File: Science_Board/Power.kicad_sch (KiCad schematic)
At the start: 57 parts, among them IC1 TCKE603RA, IC2 TCKE603RA, IC3 TCKE603RM, J21 Molex_Megafit_02, J22 Molex_Megafit_02, J3 Molex_Megafit_02, J4 Molex_Megafit_02, Q1 BS250, Q2 NMOS, Q3 NMOS, Q4 NMOS, U1 AP63205WU

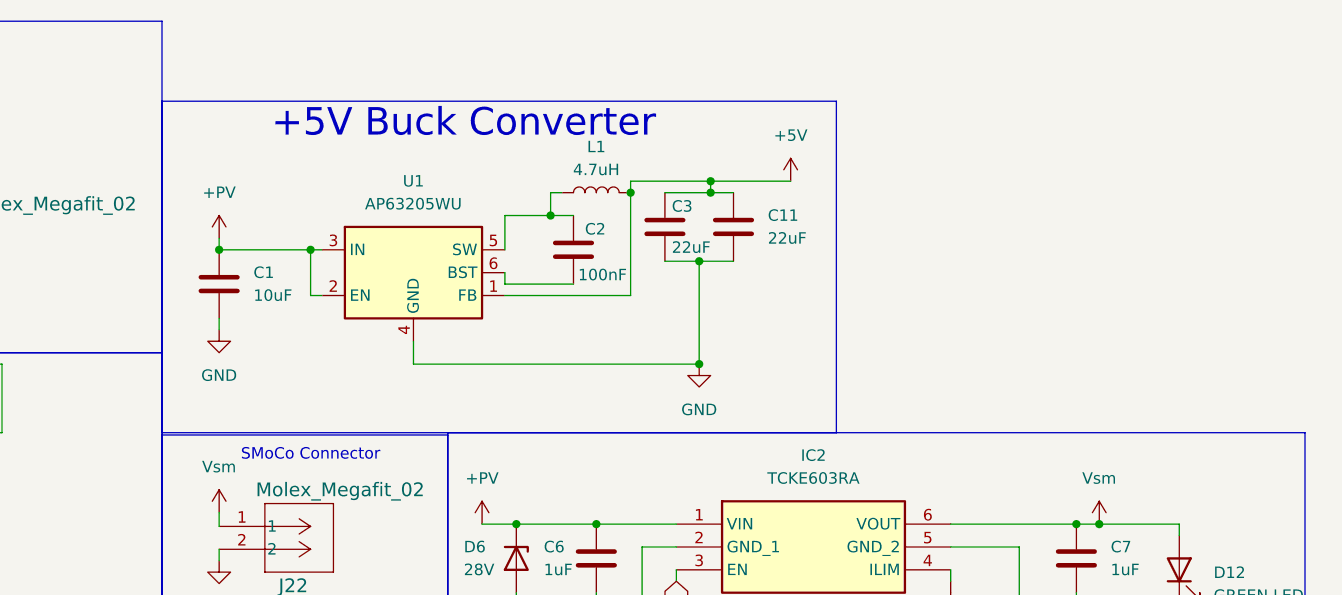
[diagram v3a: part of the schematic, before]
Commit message: changed the buck to the correct footprint
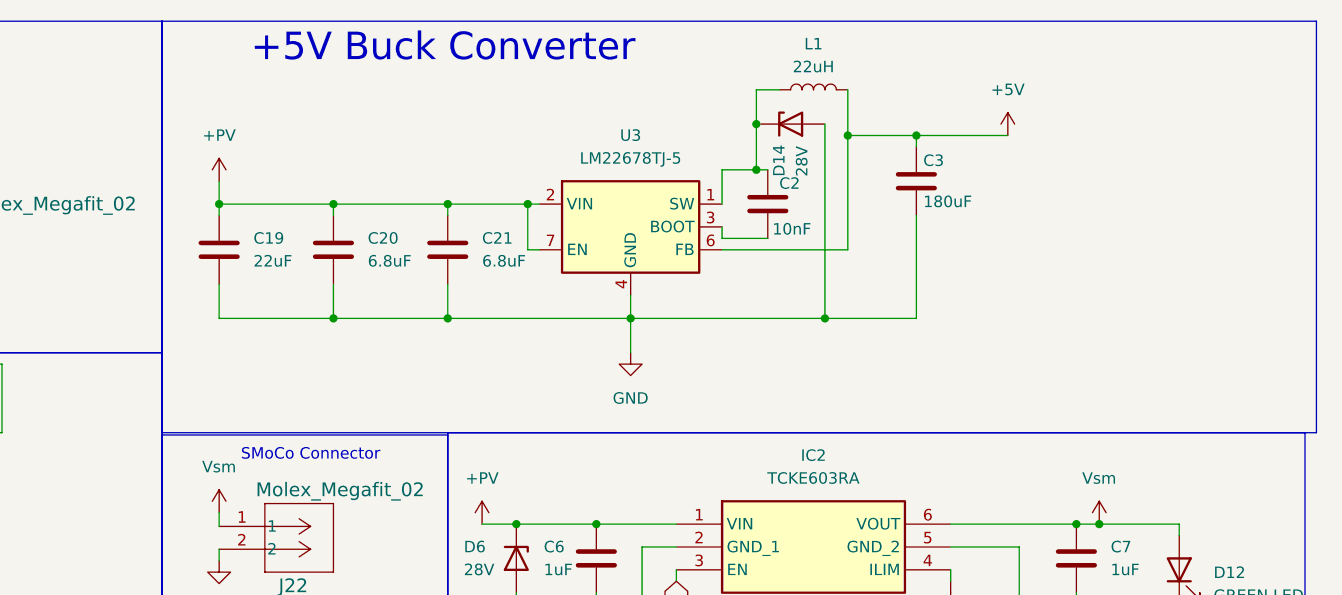
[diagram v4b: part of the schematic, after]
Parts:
- removed C1: 10uF, Capacitor_SMD:C_0603_1608Metric_Pad1.08x0.95mm_HandSolder, symbol Device:C
- removed C11: 22uF, Capacitor_SMD:C_0603_1608Metric_Pad1.08x0.95mm_HandSolder, symbol Device:C
- removed U1: AP63205WU, Package_TO_SOT_SMD:TSOT-23-6, symbol Regulator_Switching:AP63205WU
- added C19: 22uF, Capacitor_SMD:C_0603_1608Metric_Pad1.08x0.95mm_HandSolder, symbol Device:C
- added C20, C21: 6.8uF, Capacitor_SMD:C_0603_1608Metric_Pad1.08x0.95mm_HandSolder, symbol Device:C
- added D14: 28V, Diode_SMD:D_SOD-123, symbol Device:D_Zener
- added U3: LM22678TJ-5, Package_TO_SOT_SMD:TO-263-7_TabPin8, symbol Regulator_Switching:LM22678TJ-5
- C2: value 100nF -> 10nF
- C3: value 22uF -> 180uF
- L1: value 4.7uH -> 22uH
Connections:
- net +5V: now also U3.6 (FB)
- net +PV: now also C19.1, C20.1, C21.1, U3.2 (VIN), U3.7 (EN)
- net GND: now also C19.2, C20.2, C21.2, D14.2 (A), U3.4 (GND), U3.8 (GND)
- net at C2.1, L1.1: now also D14.1 (K), U3.1 (SW)
- net at C2.2: now also U3.3 (BOOT)
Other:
- moved on the sheet: C2, C3, L1

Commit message: real inductor
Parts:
- L1: value 22uH -> 6.8uH; footprint Inductor_SMD:L_0603_1608Metric_Pad1.05x0.95mm_HandSolder -> Inductor_SMD:L_Bourns_SRN8040TA
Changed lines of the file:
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@@
 			)
 		)
-		(property "Value" "22uH"
+		(property "Value" "6.8uH"
 			(at 228.6 17.78 90)
 			(show_name no)
@@
 			)
 		)
-		(property "Footprint" "Inductor_SMD:L_0603_1608Metric_Pad1.05x0.95mm_HandSolder"
+		(property "Footprint" "Inductor_SMD:L_Bourns_SRN8040TA"
 			(at 228.6 20.32 0)
 			(hide yes)
@@
 			)
 		)
-		(property "Datasheet" ""
+		(property "Datasheet" "https://www.digikey.com/en/products/detail/bourns-inc/SRN8040TA-6R8M/6155128?s=N4IgjCBcoEwAwA4DsVQGMoDMCGAbAzgKYA0IA9lANogCsAdAGwAEArQBIin0ysdd0BmXp1qCALMP4T2I%2BjUmikC%2BgmV0AnAuYzSDOmC10eOkHqEm90vqbryLjQ0vur7mk044BdUgAcALlAgAKoAdgCWfgDymACyhNj4AK4AToQgAL6k8AgIqCAYkDgEJORUogYAgrKCTFXeIP6BoRHRcQkpaZkgALQQ0PlYeESkFJDUYGC5nuldNHk%2BUGC%2BC5AwNDNAA"
 			(at 228.6 20.32 0)
 			(hide yes)

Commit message: fix mosfet
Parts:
- Q1: footprint Package_TO_SOT_THT:TO-92_Inline -> Package_TO_SOT_SMD:SOT-223
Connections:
- net at D1.2 (A), R1.2: now also Q1.1 (G); no longer Q1.2 (G)
- net at J21.1: now also Q1.2 (D), Q1.4 (D); no longer Q1.1 (D)
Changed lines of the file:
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@@
 	)
 	(junction
+		(at 132.08 58.42)
+		(diameter 0)
+		(color 0 0 0 0)
+	)
+	(junction
 		(at 111.76 64.77)
 		(diameter 0)
@@
 	(wire
 		(pts
+			(xy 132.08 55.88) (xy 132.08 58.42)
+		)
+		(stroke
+			(width 0)
+			(type default)
+		)
+	)
+	(wire
+		(pts
 			(xy 191.77 68.58) (xy 195.58 68.58)
 		)
@@
 			)
 		)
-		(property "Footprint" "Package_TO_SOT_THT:TO-92_Inline"
+		(property "Footprint" "Package_TO_SOT_SMD:SOT-223"
 			(at 125.095 55.88 0)
 			(hide yes)
@@
 			)
 		)
-		(property "Datasheet" "http://www.vishay.com/docs/70209/70209.pdf"
+		(property "Datasheet" "https://www.digikey.com/en/products/detail/onsemi/NDT452AP/458901"
 			(at 123.19 55.88 0)
 			(hide yes)
@@
 		(pin "1"
 		)
+		(pin "2"
+		)
+		(pin "4"
+		)
 		(instances

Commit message: added temp connector =
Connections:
- net +PV: no longer J3.1, J4.1
- net +Vpre: now reaches J21.1, Q1.2 (D), Q1.4 (D)
- net +Vpre: now also J3.1, J4.1
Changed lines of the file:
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@@
 	)
 	(junction
+		(at 106.68 30.48)
+		(diameter 0)
+		(color 0 0 0 0)
+	)
+	(junction
 		(at 140.97 149.86)
 		(diameter 0)
@@
 	(wire
 		(pts
+			(xy 106.68 26.67) (xy 106.68 30.48)
+		)
+		(stroke
+			(width 0)
+			(type default)
+		)
+	)
+	(wire
+		(pts
 			(xy 16.51 114.3) (xy 16.51 118.11)
 		)
@@
 	)
 	(symbol
+		(lib_id "power:VCC")
+		(at 83.82 115.57 0)
+		(unit 1)
+		(body_style 1)
+		(exclude_from_sim no)
+		(in_bom yes)
+		(on_board yes)
+		(in_pos_files yes)
+		(dnp no)
+		(property "Reference" "#PWR0124"
+			(at 83.82 119.38 0)
+			(hide yes)
+			(show_name no)
+			(do_not_autoplace no)
+			(effects
+				(font
+					(size 1.27 1.27)
+				)
+			)
+		)
+		(property "Value" "+Vpre"
+			(at 80.518 111.76 0)
+			(show_name no)
+			(do_not_autoplace no)
+			(effects
+				(font
+					(size 1.27 1.27)
+				)
+				(justify left)
+			)
+		)
+		(property "Footprint" "MRDT_Connectors:MOLEX_MegaFit_02_Horizontal"
+			(at 83.82 115.57 0)
+			(hide yes)
+			(show_name no)
+			(do_not_autoplace no)
+			(effects
+				(font
+					(size 1.27 1.27)
+				)
+			)
+		)
+		(property "Datasheet" ""
+			(at 83.82 115.57 0)
+			(hide yes)
+			(show_name no)
+			(do_not_autoplace no)
+			(effects
+				(font
+					(size 1.27 1.27)
+				)
+			)
+		)
+		(property "Description" "Power symbol creates a global label with name \"VCC\""
+			(at 83.82 115.57 0)
+			(hide yes)
+			(show_name no)
+			(do_not_autoplace no)
+			(effects
+				(font
+					(size 1.27 1.27)
+				)
+			)
+		)
+		(pin "1"
+		)
+		(instances
+			(project "Science_Board"
+				(path "/4f5c5f7f-4385-4de2-96ca-2ae741ebf691/6219bf49-5574-4710-86f4-9f93da84ad76"
+					(reference "#PWR0124")
+					(unit 1)
+				)
+			)
+		)
+	)
+	(symbol
 		(lib_id "Device:R_US")
 		(at 38.1 45.72 0)
@@
 	)
 	(symbol
-		(lib_id "power:VCC")
-		(at 83.82 115.57 0)
+		(lib_id "Simulation_SPICE:NMOS")
+		(at 35.56 77.47 0)
 		(unit 1)
 		(body_style 1)
@@
 		(dnp no)
 		(fields_autoplaced yes)
-		(property "Reference" "#PWR046"
-			(at 83.82 119.38 0)
-			(hide yes)
+		(property "Reference" "Q4"
+			(at 41.91 76.1999 0)
 			(show_name no)
 			(do_not_autoplace no)
@@
 					(size 1.27 1.27)
 				)
+				(justify left)
 			)
 		)
-		(property "Value" "+PV"
-			(at 83.82 110.49 0)
+		(property "Value" "NMOS"
+			(at 41.91 78.7399 0)
 			(show_name no)
 			(do_not_autoplace no)
@@
 					(size 1.27 1.27)
 				)
+				(justify left)
 			)
 		)
-		(property "Footprint" "MRDT_Connectors:MOLEX_MegaFit_02_Horizontal"
-			(at 83.82 115.57 0)
+		(property "Footprint" "Package_TO_SOT_SMD:SOT-23-3"
+			(at 40.64 74.93 0)
 			(hide yes)
 			(show_name no)
@@
 			)
 		)
-		(property "Datasheet" ""
-			(at 83.82 115.57 0)
+		(property "Datasheet" "https://ngspice.sourceforge.io/docs/ngspice-html-manual/manual.xhtml#cha_MOSFETs"
+			(at 35.56 90.17 0)
 			(hide yes)
 			(show_name no)
@@
 			)
 		)
-		(property "Description" "Power symbol creates a global label with name \"VCC\""
-			(at 83.82 115.57 0)
+		(property "Description" "N-MOSFET transistor, drain/source/gate"
+			(at 35.56 77.47 0)
 			(hide yes)
 			(show_name no)
@@
 			)
 		)
-		(pin "1"
-		)
-		(instances
-			(project "Science_Board"
-				(path "/4f5c5f7f-4385-4de2-96ca-2ae741ebf691/6219bf49-5574-4710-86f4-9f93da84ad76"
-					(reference "#PWR046")
-					(unit 1)
-				)
-			)
-		)
-	)
-	(symbol
-		(lib_id "Simulation_SPICE:NMOS")
-		(at 35.56 77.47 0)
-		(unit 1)
-		(body_style 1)
-		(exclude_from_sim no)
-		(in_bom yes)
-		(on_board yes)
-		(in_pos_files yes)
-		(dnp no)
-		(fields_autoplaced yes)
-		(property "Reference" "Q4"
-			(at 41.91 76.1999 0)
+		(property "Sim.Device" "NMOS"
+			(at 35.56 94.615 0)
+			(hide yes)
 			(show_name no)
 			(do_not_autoplace no)
@@
 					(size 1.27 1.27)
 				)
-				(justify left)
 			)
 		)
-		(property "Value" "NMOS"
-			(at 41.91 78.7399 0)
+		(property "Sim.Type" "VDMOS"
+			(at 35.56 96.52 0)
+			(hide yes)
 			(show_name no)
 			(do_not_autoplace no)
@@
 					(size 1.27 1.27)
 				)
-				(justify left)
 			)
 		)
-		(property "Footprint" "Package_TO_SOT_SMD:SOT-23-3"
-			(at 40.64 74.93 0)
+		(property "Sim.Pins" "1=D 2=G 3=S"
+			(at 35.56 92.71 0)
 			(hide yes)
 			(show_name no)
@@
 			)
 		)
-		(property "Datasheet" "https://ngspice.sourceforge.io/docs/ngspice-html-manual/manual.xhtml#cha_MOSFETs"
-			(at 35.56 90.17 0)
+		(pin "1"
+		)
+		(pin "3"
+		)
+		(pin "2"
+		)
+		(instances
+			(project "Science_Board"
+				(path "/4f5c5f7f-4385-4de2-96ca-2ae741ebf691/6219bf49-5574-4710-86f4-9f93da84ad76"
+					(reference "Q4")
+					(unit 1)
+				)
+			)
+		)
+	)
+	(symbol
+		(lib_id "power:VCC")
+		(at 38.1 71.12 0)
+		(unit 1)
+		(body_style 1)
+		(exclude_from_sim no)
+		(in_bom yes)
+		(on_board yes)
+		(in_pos_files yes)
+		(dnp no)
+		(fields_autoplaced yes)
+		(property "Reference" "#PWR091"
+			(at 38.1 74.93 0)
 			(hide yes)
 			(show_name no)
@@
 			)
 		)
-		(property "Description" "N-MOSFET transistor, drain/source/gate"
-			(at 35.56 77.47 0)
-			(hide yes)
+		(property "Value" "+3V3"
+			(at 38.1 66.04 0)
 			(show_name no)
 			(do_not_autoplace no)
@@
 			)
 		)
-		(property "Sim.Device" "NMOS"
-			(at 35.56 94.615 0)
+		(property "Footprint" ""
+			(at 38.1 71.12 0)
 			(hide yes)
 			(show_name no)
@@
 			)
 		)
-		(property "Sim.Type" "VDMOS"
-			(at 35.56 96.52 0)
+		(property "Datasheet" ""
+			(at 38.1 71.12 0)
 			(hide yes)
 			(show_name no)
@@
 			)
 		)
-		(property "Sim.Pins" "1=D 2=G 3=S"
-			(at 35.56 92.71 0)
+		(property "Description" "Power symbol creates a global label with name \"VCC\""
+			(at 38.1 71.12 0)
 			(hide yes)
 			(show_name no)
@@
 		(pin "1"
 		)
-		(pin "3"
-		)
-		(pin "2"
-		)
 		(instances
 			(project "Science_Board"
 				(path "/4f5c5f7f-4385-4de2-96ca-2ae741ebf691/6219bf49-5574-4710-86f4-9f93da84ad76"
-					(reference "Q4")
+					(reference "#PWR091")
 					(unit 1)
 				)
@@
 	(symbol
 		(lib_id "power:VCC")
-		(at 38.1 71.12 0)
+		(at 106.68 26.67 0)
 		(unit 1)
 		(body_style 1)
@@
 		(in_pos_files yes)
 		(dnp no)
-		(fields_autoplaced yes)
-		(property "Reference" "#PWR091"
-			(at 38.1 74.93 0)
+		(property "Reference" "#PWR0128"
+			(at 106.68 30.48 0)
 			(hide yes)
 			(show_name no)
@@
 			)
 		)
-		(property "Value" "+3V3"
-			(at 38.1 66.04 0)
+		(property "Value" "+Vpre"
+			(at 103.378 22.86 0)
 			(show_name no)
 			(do_not_autoplace no)
@@
 					(size 1.27 1.27)
 				)
+				(justify left)
 			)
 		)
-		(property "Footprint" ""
-			(at 38.1 71.12 0)
+		(property "Footprint" "MRDT_Connectors:MOLEX_MegaFit_02_Horizontal"
+			(at 106.68 26.67 0)
 			(hide yes)
 			(show_name no)
@@
 		)
 		(property "Datasheet" ""
-			(at 38.1 71.12 0)
+			(at 106.68 26.67 0)
 			(hide yes)
 			(show_name no)
@@
 		)
 		(property "Description" "Power symbol creates a global label with name \"VCC\""
-			(at 38.1 71.12 0)
+			(at 106.68 26.67 0)
 			(hide yes)
 			(show_name no)
@@
 			(project "Science_Board"
 				(path "/4f5c5f7f-4385-4de2-96ca-2ae741ebf691/6219bf49-5574-4710-86f4-9f93da84ad76"
-					(reference "#PWR091")
+					(reference "#PWR0128")
 					(unit 1)
 				)
@@
 		(in_pos_files yes)
 		(dnp no)
-		(fields_autoplaced yes)
-		(property "Reference" "#PWR043"
+		(property "Reference" "#PWR0127"
 			(at 120.65 118.11 0)
 			(hide yes)
@@
 			)
 		)
-		(property "Value" "+PV"
-			(at 120.65 109.22 0)
+		(property "Value" "+Vpre"
+			(at 117.348 110.49 0)
 			(show_name no)
 			(do_not_autoplace no)
@@
 					(size 1.27 1.27)
 				)
+				(justify left)
 			)
 		)
@@
 			(project "Science_Board"
 				(path "/4f5c5f7f-4385-4de2-96ca-2ae741ebf691/6219bf49-5574-4710-86f4-9f93da84ad76"
-					(reference "#PWR043")
+					(reference "#PWR0127")
 					(unit 1)
 				)

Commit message: Diode now has the correct footprint and made the mounting holes the correct distance apart
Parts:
- removed D14: 28V, Diode_SMD:D_SOD-123, symbol Device:D_Zener
- added D15: D_Schottky, Diode_SMD:D_SOD-128, symbol Device:D_Schottky
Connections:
- net GND: now also D15.2 (A)
- net at C2.1, L1.1, U3.1 (SW): now also D15.1 (K)
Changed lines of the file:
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@@
 	)
 	(junction
-		(at 222.25 24.13)
-		(diameter 0)
-		(color 0 0 0 0)
-	)
-	(junction
 		(at 260.35 68.58)
 		(diameter 0)
@@
 	)
 	(junction
+		(at 222.25 24.13)
+		(diameter 0)
+		(color 0 0 0 0)
+	)
+	(junction
 		(at 186.69 110.49)
 		(diameter 0)
@@
 	(wire
 		(pts
-			(xy 222.25 20.32) (xy 222.25 24.13)
-		)
-		(stroke
-			(width 0)
-			(type default)
-		)
-	)
-	(wire
-		(pts
 			(xy 232.41 20.32) (xy 232.41 25.4)
 		)
@@
 	(wire
 		(pts
-			(xy 222.25 24.13) (xy 222.25 29.21)
+			(xy 222.25 20.32) (xy 222.25 24.13)
 		)
 		(stroke
@@
 	(wire
 		(pts
+			(xy 222.25 24.13) (xy 222.25 29.21)
+		)
+		(stroke
+			(width 0)
+			(type default)
+		)
+	)
+	(wire
+		(pts
 			(xy 130.81 154.94) (xy 130.81 156.21)
 		)
@@
 	)
 	(symbol
+		(lib_id "Device:D_Schottky")
+		(at 226.06 24.13 0)
+		(unit 1)
+		(body_style 1)
+		(exclude_from_sim no)
+		(in_bom yes)
+		(on_board yes)
+		(in_pos_files yes)
+		(dnp no)
+		(property "Reference" "D15"
+			(at 225.806 21.59 0)
+			(show_name no)
+			(do_not_autoplace no)
+			(effects
+				(font
+					(size 1.27 1.27)
+				)
+			)
+		)
+		(property "Value" "D_Schottky"
+			(at 225.806 27.178 0)
+			(show_name no)
+			(do_not_autoplace no)
+			(effects
+				(font
+					(size 1.27 1.27)
+				)
+			)
+		)
+		(property "Footprint" "Diode_SMD:D_SOD-128"
+			(at 226.06 24.13 0)
+			(hide yes)
+			(show_name no)
+			(do_not_autoplace no)
+			(effects
+				(font
+					(size 1.27 1.27)
+				)
+			)
+		)
+		(property "Datasheet" ""
+			(at 226.06 24.13 0)
+			(hide yes)
+			(show_name no)
+			(do_not_autoplace no)
+			(effects
+				(font
+					(size 1.27 1.27)
+				)
+			)
+		)
+		(property "Description" "Schottky diode"
+			(at 226.06 24.13 0)
+			(hide yes)
+			(show_name no)
+			(do_not_autoplace no)
+			(effects
+				(font
+					(size 1.27 1.27)
+				)
+			)
+		)
+		(pin "1"
+		)
+		(pin "2"
+		)
+		(instances
+			(project "Science_Board"
+				(path "/4f5c5f7f-4385-4de2-96ca-2ae741ebf691/6219bf49-5574-4710-86f4-9f93da84ad76"
+					(reference "D15")
+					(unit 1)
+				)
+			)
+		)
+	)
+	(symbol
 		(lib_id "Device:D_Zener")
 		(at 118.11 63.5 270)
@@
 					(unit 1)
 				)
-			)
-		)
-	)
-	(symbol
-		(lib_id "Device:D_Zener")
-		(at 226.06 24.13 0)
-		(unit 1)
-		(body_style 1)
-		(exclude_from_sim no)
-		(in_bom yes)
-		(on_board yes)
-		(in_pos_files yes)
-		(dnp no)
-		(property "Reference" "D14"
-			(at 224.79 29.972 90)
-			(show_name no)
-			(do_not_autoplace no)
-			(effects
-				(font
-					(size 1.27 1.27)
-				)
-				(justify left)
-			)
-		)
-		(property "Value" "28V"
-			(at 227.33 29.972 90)
-			(show_name no)
-			(do_not_autoplace no)
-			(effects
-				(font
-					(size 1.27 1.27)
-				)
-				(justify left)
-			)
-		)
-		(property "Footprint" "Diode_SMD:D_SOD-123"
-			(at 226.06 24.13 0)
-			(hide yes)
-			(show_name no)
-			(do_not_autoplace no)
-			(effects
-				(font
-					(size 1.27 1.27)
-				)
-			)
-		)
-		(property "Datasheet" ""
-			(at 226.06 24.13 0)
-			(hide yes)
-			(show_name no)
-			(do_not_autoplace no)
-			(effects
-				(font
-					(size 1.27 1.27)
-				)
-			)
-		)
-		(property "Description" "Zener diode"
-			(at 226.06 24.13 0)
-			(hide yes)
-			(show_name no)
-			(do_not_autoplace no)
-			(effects
-				(font
-					(size 1.27 1.27)
-				)
-			)
-		)
-		(pin "1"
-		)
-		(pin "2"
-		)
-		(instances
-			(project "Science_Board"
-				(path "/4f5c5f7f-4385-4de2-96ca-2ae741ebf691/6219bf49-5574-4710-86f4-9f93da84ad76"
-					(reference "D14")
-					(unit 1)
-				)
